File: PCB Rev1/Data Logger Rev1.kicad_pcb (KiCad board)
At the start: 2 copper layers, 4 parts, among them J1 MICRO_SD, U1 SAM-M10Q, U2 ESP32-PICO-V3-ZERO, U3 AP22653QW6-7

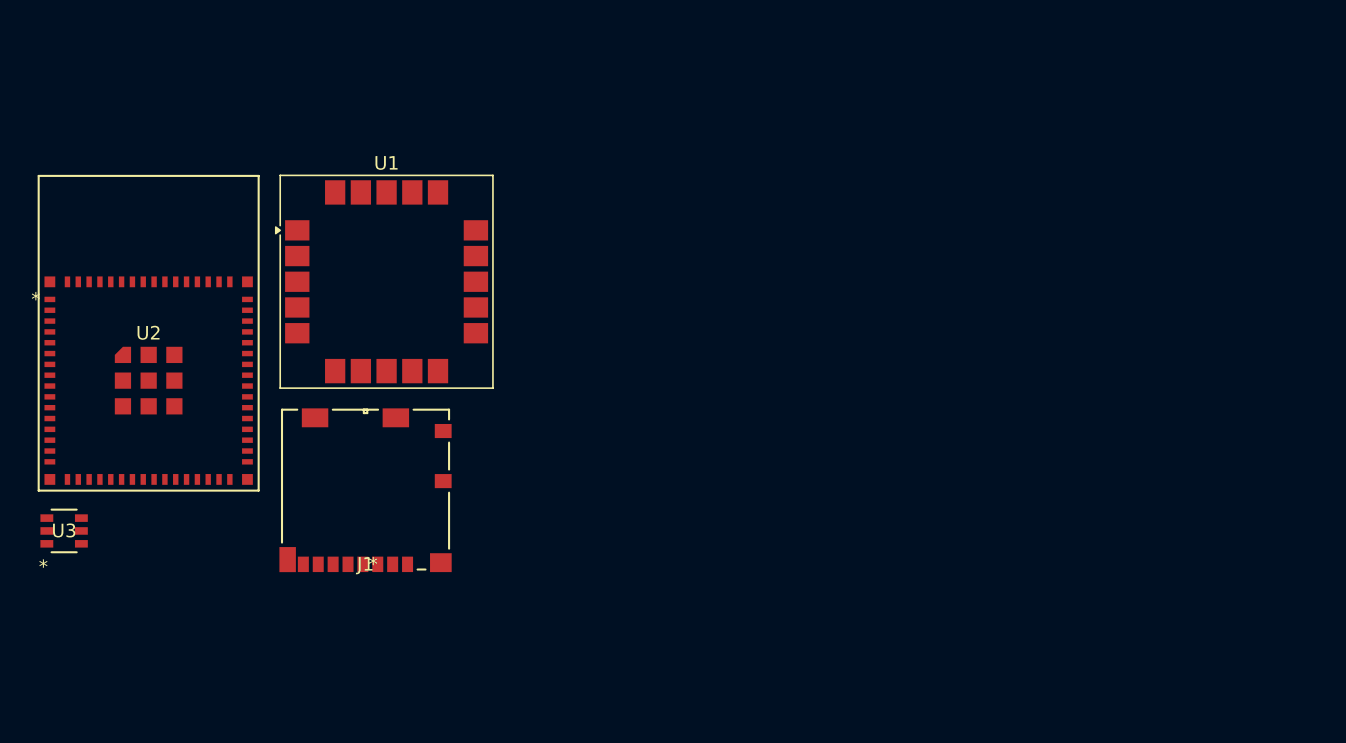
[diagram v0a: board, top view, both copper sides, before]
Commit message: aggregated SD card and switch, updated power architecture to use 5V, added TVS diode array
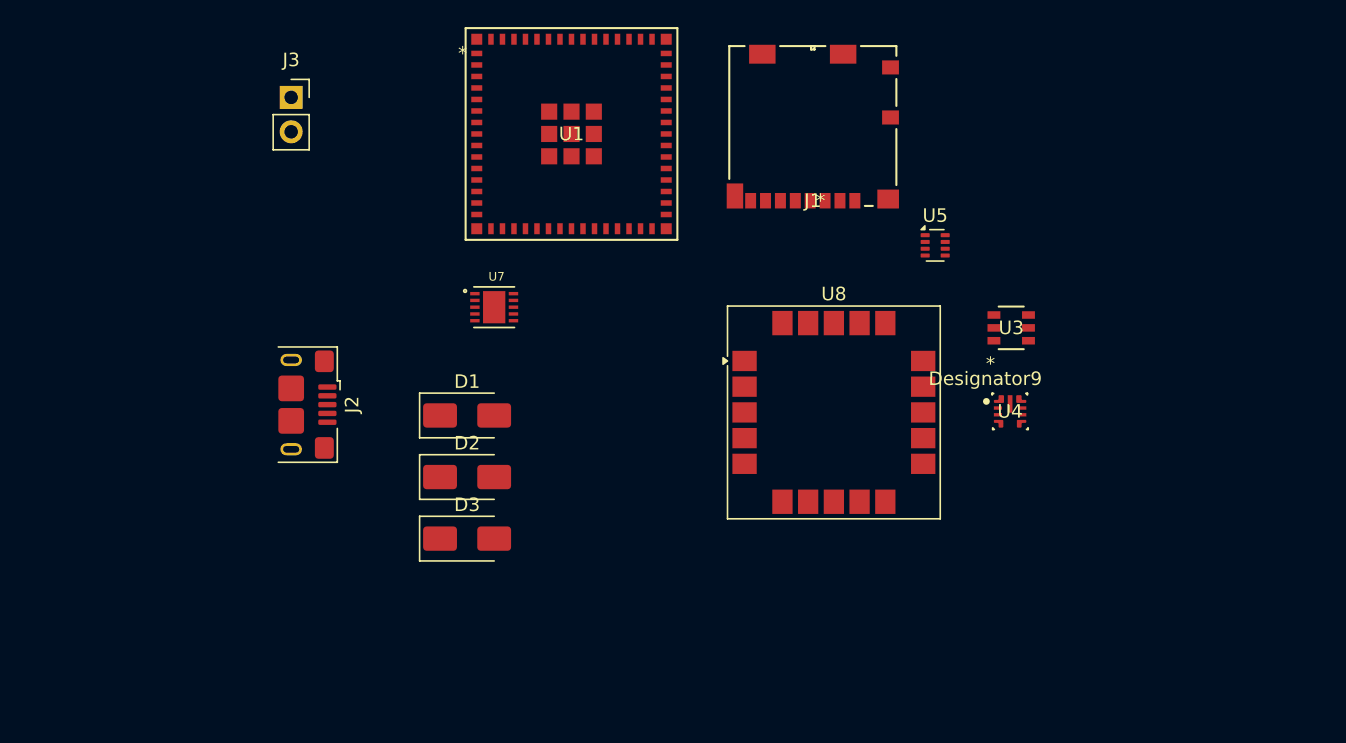
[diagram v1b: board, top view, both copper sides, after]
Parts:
- removed U2: ESP32-PICO-V3-ZERO, footprints:ESP32-PICO-V3-ZERO_EXP
- added D1: TVS, Diode_SMD:D_SMA, F.Cu at (144.5, 100.0)
- added D2: TVS, Diode_SMD:D_SMA, F.Cu at (144.5, 104.5)
- added D3: TVS, Diode_SMD:D_SMA, F.Cu at (144.5, 109.1)
- added J2: USB_B_Micro, Connector_USB:USB_Micro-B_Amphenol_10118193-0001LF_Horizontal, F.Cu at (131.5, 99.2)
- added J3: Conn_01x02_Socket, Connector_PinSocket_2.54mm:PinSocket_1x02_P2.54mm_Vertical, F.Cu at (131.5, 76.5)
- added U4: LMR43620MSC3RPERQ1, footprints:RPE0009A-MFG, F.Cu at (184.6, 99.7)
- added U5: TPS2116DRL, Package_TO_SOT_SMD:SOT-583-8, F.Cu at (179.1, 87.4)
- added U7: LT3042EDD_PBF, footprints:VREG_LT3042EDD_PBF, F.Cu at (146.5, 92.0)
- added U8: SAM-M10Q, RF_GPS:ublox_SAM-M8Q, F.Cu at (171.6, 99.8)
- U1: value SAM-M10Q -> ESP32-S3-MINI-1U-N8; footprint RF_GPS:ublox_SAM-M8Q -> footprints:ESP32-S3-MINI-1U_EXP
- moved U3 71.6 mm to (184.7, 93.5)
- moved J1 42.6 mm to (170.0, 78.6)
- moved U1 17.5 mm to (152.2, 79.2)
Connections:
- J1 pad 1: unconnected-(J1-DAT2-Pad1) -> /GPIO42
- J1 pad 10: unconnected-(J1-SW_DETECT-Pad10) -> GND
- J1 pad 2: unconnected-(J1-CD/DAT3-Pad2) -> /GPIO35
- J1 pad 3: unconnected-(J1-CMD-Pad3) -> /GPIO37
- J1 pad 4: unconnected-(J1-VDD-Pad4) -> /power_switch/out
- J1 pad 5: unconnected-(J1-CLK-Pad5) -> /GPIO36
- J1 pad 6: unconnected-(J1-VSS-Pad6) -> GND
- J1 pad 7: unconnected-(J1-DAT0-Pad7) -> /GPIO38
- J1 pad 8: unconnected-(J1-DAT1-Pad8) -> /GPIO39
- J1 pad 9: unconnected-(J1-SW_DETECT-Pad9) -> /GPIO1
- U1 pad 1: Net-(U1-GND-Pad1) -> Net-(U1-GND1-Pad1)
- U1 pad 10: Net-(U1-GND-Pad1) -> unconnected-(U1-IO6-Pad10)
- U1 pad 11: Net-(U1-GND-Pad1) -> unconnected-(U1-IO7-Pad11)
- U1 pad 15: Net-(U1-GND-Pad1) -> unconnected-(U1-IO11-Pad15)
- U1 pad 16: Net-(U1-GND-Pad1) -> unconnected-(U1-IO12-Pad16)
- U1 pad 2: unconnected-(U1-VCC_IO-Pad2) -> Net-(U1-GND1-Pad1)
- U1 pad 20: Net-(U1-GND-Pad1) -> unconnected-(U1-IO16-Pad20)
- U1 pad 4: Net-(U1-GND-Pad1) -> /GPIO0
- U1 pad 5: Net-(U1-GND-Pad1) -> /GPIO1
- U1 pad 6: Net-(U1-GND-Pad1) -> unconnected-(U1-IO2-Pad6)
- U3 pad 1: unconnected-(U3-in-Pad1) -> +3.3V
- U3 pad 2: unconnected-(U3-gnd-Pad2) -> GND
- U3 pad 3: unconnected-(U3-en-Pad3) -> /power_switch/en
- U3 pad 4: unconnected-(U3-*fault-Pad4) -> Net-(U3-*fault)
- U3 pad 5: unconnected-(U3-ilim-Pad5) -> Net-(U3-ilim)
- U3 pad 6: unconnected-(U3-out-Pad6) -> /power_switch/out

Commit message: added PCB rev2!
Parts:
- removed D2: TVS, Diode_SMD:D_SMA
- removed J1: MICRO_SD, footprints:104031-0811_MOL
- removed J3: Conn_01x02_Socket, Connector_PinSocket_2.54mm:PinSocket_1x02_P2.54mm_Vertical
- removed U7: LT3042EDD_PBF, footprints:VREG_LT3042EDD_PBF
- removed U8: SAM-M10Q, RF_GPS:ublox_SAM-M8Q
- added 12V: 12V_Tractor, footprints:PHOENIX_1725656, F.Cu at (205.3, 87.8)
- added 3.3V: 3.3V, footprints:TP_245X165, F.Cu at (179.7, 119.6)
- added 5V: 5V, footprints:TP_245X165, F.Cu at (199.4, 95.8)
- added 5V|3.7V: V_BAT_IC, footprints:TP_245X165, F.Cu at (199.4, 92.5)
- added BATT: BATTERY_PLUG, footprints:PHOENIX_1725656, F.Cu at (205.3, 106.3)
- added BOOT: BOOT, footprints:TP_245X165, F.Cu at (150.7, 81.0)
- added BOOT: BOOT, footprints:SW_TL1105TF160Q, F.Cu at (159.9, 83.3)
- added C1: 10uF, footprints:CAPC3216X190N, F.Cu at (192.1, 82.3)
- added C10: 4.7uF, Capacitor_SMD:C_0603_1608Metric, F.Cu at (191.9, 94.8)
- added C11: 10uF, Capacitor_SMD:C_0805_2012Metric, F.Cu at (155.2, 115.8)
- added C12: 0.1uF, Capacitor_SMD:C_0603_1608Metric, F.Cu at (157.2, 116.1)
- added C13: 10uF, Capacitor_SMD:C_0805_2012Metric, F.Cu at (192.6, 111.2)
- added C14: 1uF, Capacitor_SMD:C_0603_1608Metric, F.Cu at (193.9, 116.3)
- added C15: 10uF, Capacitor_SMD:C_0805_2012Metric, F.Cu at (186.8, 111.2)
- added C16: 10uF, Capacitor_SMD:C_0805_2012Metric, F.Cu at (182.2, 113.4)
- added C17: 0.1uF, Capacitor_SMD:C_0603_1608Metric, F.Cu at (180.2, 113.2)
- added C18: 0.1uF, Capacitor_SMD:C_0603_1608Metric, F.Cu at (176.0, 110.9)
- added C19: 0.1uF, Capacitor_SMD:C_0603_1608Metric, F.Cu at (178.7, 102.0)
- added C2: 4.7uF, footprints:CAPC2012X150N, F.Cu at (194.5, 90.8)
- added C20: 1uF, Capacitor_SMD:C_0603_1608Metric, F.Cu at (178.7, 98.8)
- added C21: 10uF, Capacitor_SMD:C_0805_2012Metric, F.Cu at (180.7, 102.2)
- added C22: 10uF, Capacitor_SMD:C_0805_2012Metric, F.Cu at (148.9, 119.5)
- added C23: 1uF, Capacitor_SMD:C_0603_1608Metric, F.Cu at (138.2, 119.5)
- added C3: 4.7uF, footprints:CAPC2012X150N, F.Cu at (192.6, 84.8)
- added C4: 100nF, footprints:CAPC2012X94N, F.Cu at (192.6, 87.0)
- added C5: 1uF, Capacitor_SMD:C_0805_2012Metric, F.Cu at (187.9, 90.5)
- added C6: 100nF, footprints:CAPC1005X55N, F.Cu at (188.9, 88.3)
- added C7: 22uF, footprints:CAPC3216X190N, F.Cu at (186.2, 80.5)
- added C8: 10uF, Capacitor_SMD:C_0805_2012Metric, F.Cu at (194.4, 98.8)
- added C9: 4.7uF, Capacitor_SMD:C_0603_1608Metric, F.Cu at (192.4, 102.8)
- added D4: LED, LED_SMD:LED_0603_1608Metric, F.Cu at (183.7, 94.5)
- added D5: LED, LED_SMD:LED_0603_1608Metric, F.Cu at (183.7, 103.5)
- added D6: LED, LED_SMD:LED_0603_1608Metric, F.Cu at (183.9, 99.0)
- added EN: EN, footprints:TP_245X165, F.Cu at (181.1, 91.6)
- added FB1: FerriteBead, Resistor_SMD:R_0603_1608Metric, F.Cu at (143.4, 119.8)
- added G***: LOGO, footprints:strawberry_silkscreen_small, F.Cu at (124.6, 89.5)
- added J4: MICRO_SD, footprints:104031-0811_MOL, F.Cu at (164.6, 113.9)
- added JP1: Jumper_2_Open, Jumper:SolderJumper-2_P1.3mm_Open_RoundedPad1.0x1.5mm, F.Cu at (154.7, 119.2)
- added L1: 330nH, footprints:WE-MAPI_2510, F.Cu at (196.1, 86.3)
- added L2: 2.2uH, Inductor_SMD:L_TDK_VLS6045EX_VLS6045AF, F.Cu at (185.0, 85.2)
- added R1: 10, footprints:RES_ERJ3EKF10R0V, F.Cu at (194.3, 89.0)
- added R10: 10k, Resistor_SMD:R_0402_1005Metric, F.Cu at (157.2, 103.5)
- added R11: 10k, Resistor_SMD:R_0603_1608Metric, F.Cu at (175.2, 117.4)
- added R12: 40k, footprints:RESC1005X35N, F.Cu at (173.2, 113.7)
- added R13: 10k, Resistor_SMD:R_0603_1608Metric, F.Cu at (180.5, 98.8)
- added R14: 10k, Resistor_SMD:R_0603_1608Metric, F.Cu at (178.7, 105.3)
- added R15: 10k, Resistor_SMD:R_0402_1005Metric, F.Cu at (166.7, 105.7)
- added R2: 1k, Resistor_SMD:R_0603_1608Metric, F.Cu at (189.9, 103.5)
- added R3: 10k, Resistor_SMD:R_0603_1608Metric, F.Cu at (188.1, 103.5)
- added R4: 470, Resistor_SMD:R_0603_1608Metric, F.Cu at (185.9, 94.0)
- added R5: 470, Resistor_SMD:R_0603_1608Metric, F.Cu at (185.7, 103.5)
- added R6: 470, Resistor_SMD:R_0603_1608Metric, F.Cu at (185.7, 97.3)
- added R7: 10k, Resistor_SMD:R_0402_1005Metric, F.Cu at (157.7, 101.0)
- added R8: 10k, Resistor_SMD:R_0402_1005Metric, F.Cu at (169.9, 105.8)
- added R9: 10k, Resistor_SMD:R_0402_1005Metric, F.Cu at (157.2, 106.5)
- added REF**: MountingHole_2.5mm_Pad, MountingHole:MountingHole_2.5mm_Pad, F.Cu at (120.7, 81.8)
- added REF**: MountingHole_2.5mm_Pad, MountingHole:MountingHole_2.5mm_Pad, F.Cu at (120.7, 118.3)
- added REF**: MountingHole_2.5mm_Pad, MountingHole:MountingHole_2.5mm_Pad, F.Cu at (202.9, 118.0)
- added RST: RESET, footprints:SW_TL1105TF160Q, F.Cu at (177.2, 83.3)
- added TH1: 10k, Resistor_SMD:R_0402_1005Metric, F.Cu at (187.9, 95.2)
- added TP3: RXD, footprints:TP_245X165, F.Cu at (157.9, 91.0)
- added TP6: TXD, footprints:TP_245X165, F.Cu at (157.9, 93.3)
- added U2: MCP73871-2CCI_ML, footprints:QFN50P400X400X100-21N, F.Cu at (189.7, 99.0)
- added U6: SAM-M10Q, RF_GPS:ublox_SAM-M8Q, F.Cu at (138.8, 99.8)
- added V_BAT: V_BAT, footprints:TP_245X165, F.Cu at (199.4, 99.0)
- D1: footprint Diode_SMD:D_SMA -> Diode_SMD:D_SOD-523
- D3: value TVS -> D_Schottky; footprint Diode_SMD:D_SMA -> footprints:CR_SMP_DO-220AA_VIS
- U1: value ESP32-S3-MINI-1U-N8 -> LMR43620MSC5-Q1RPE; footprint footprints:ESP32-S3-MINI-1U_EXP -> footprints:RPE0009A-MFG
- U3: value AP22653QW6-7 -> TPS7A4700RGWR; footprint footprints:SOT26-A1-AP22653Q_DIO -> footprints:QFN65P500X500X100-21N
- U4: value LMR43620MSC3RPERQ1 -> AP22653QW6-7; footprint footprints:RPE0009A-MFG -> footprints:SOT26-A1-AP22653Q_DIO
- U5: value TPS2116DRL -> ESP32-S3-MINI-1U-N8; footprint Package_TO_SOT_SMD:SOT-583-8 -> footprints:ESP32-S3-MINI-1U_EXP
- moved D3 58.3 mm to (196.1, 81.9)
- moved D1 52.6 mm to (193.1, 79.8), turned to 180 degrees
- moved J2 41.7 mm to (168.6, 80.3), turned to 180 degrees
- moved U1 40.4 mm to (191.2, 89.6), turned to 180 degrees
- moved U3 23.3 mm to (189.7, 116.3)
- moved U4 16.1 mm to (176.7, 113.8), turned to 180 degrees
- moved U5 13.1 mm to (169.3, 96.1), turned to 180 degrees
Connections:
- D1 pad 1: GND -> +12V
- D1 pad 2: /GPIO19 -> GND
- D3 pad 1: GND -> +12V
- D3 pad 2: +12V -> /12V_5V BUCK/PI_IN
- J2 pad 1: +12V -> +5V
- J2 pad 2: /GPIO19 -> /D-
- J2 pad 3: /GPIO20 -> /D+
- U1 pad 1: Net-(U1-GND1-Pad1) -> GND
- U1 pad 2: Net-(U1-GND1-Pad1) -> unconnected-(U1-PGOOD-Pad2)
- U1 pad 3: unconnected-(U1-3V3-Pad3) -> /12V_5V BUCK/V_IN_BUCK
- U1 pad 4: /GPIO0 -> /12V_5V BUCK/V_IN_BUCK
- U1 pad 5: /GPIO1 -> Net-(U1-SW)
- U1 pad 6: unconnected-(U1-IO2-Pad6) -> Net-(U1-BOOT)
- U1 pad 7: unconnected-(U1-IO3-Pad7) -> Net-(U1-VCC)
- U1 pad 8: unconnected-(U1-IO4-Pad8) -> +5V
- U1 pad 9: unconnected-(U1-IO5-Pad9) -> GND
- U3 pad 1: +3.3V -> /5V_3.3V LDO/3.3V
- U3 pad 2: GND -> (no net)
- U3 pad 3: /power_switch/en -> /5V_3.3V LDO/3.3V
- U3 pad 4: Net-(U3-*fault) -> unconnected-(U3-6P4V2-Pad4)
- U3 pad 5: Net-(U3-ilim) -> unconnected-(U3-6P4V1-Pad5)
- U3 pad 6: /power_switch/out -> unconnected-(U3-3P2V-Pad6)
- U4 pad 1: GND -> /5V_3.3V LDO/3.3V
- U4 pad 2: unconnected-(U4-PGOOD-Pad2) -> GND
- U4 pad 3: +12V -> /EN
- U4 pad 4: +12V -> Net-(U4-*FAULT)
- U4 pad 6: Net-(U4-BOOT) -> /EN_SWITCH/V_OUT
- U5 pad 1: unconnected-(U5-GND-Pad1) -> GND
- U5 pad 2: Net-(U5-VOUT-Pad2) -> GND
- U5 pad 3: /GPS Module/3.6V -> /5V_3.3V LDO/3.3V
- U5 pad 4: unconnected-(U5-PR1-Pad4) -> Net-(U5-IO0)
- U5 pad 7: Net-(U5-VOUT-Pad2) -> /EN
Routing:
- net /EN_SWITCH/V_OUT: track 0.00 -> 74.1 mm, vias 0 -> 6
- net /5V_3.3V LDO/3.3V: track 0.00 -> 56.7 mm, vias 0 -> 6
- net Net-(U5-IO0): track 0.00 -> 48.3 mm, vias 0 -> 3
- net /EXTINT: track 0.00 -> 47.8 mm, vias 0 -> 2
- net /1SEC: track 0.00 -> 46.8 mm, vias 0 -> 2
- net Net-(U6-VCC): track 0.00 -> 44.8 mm
- net +5V: track 0.00 -> 41.2 mm, vias 0 -> 9
- net Net-(U5-EN): track 0.00 -> 40.4 mm, vias 0 -> 3
- net Net-(JP1-B): track 0.00 -> 35.8 mm
- net /DAT1: track 0.00 -> 32.7 mm, vias 0 -> 2
- net /DAT3: track 0.00 -> 30.6 mm, vias 0 -> 2
- net /DAT0: track 0.00 -> 30.0 mm, vias 0 -> 2
- net /CMD: track 0.00 -> 29.3 mm, vias 0 -> 2
- net /DAT2: track 0.00 -> 29.2 mm, vias 0 -> 2
- net /CLK: track 0.00 -> 22.7 mm
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- added copper zone on In2.Cu, net +5V
- added copper zone on F.Cu, net /12V_5V BUCK/PI_IN
- added copper zone on F.Cu, net /12V_5V BUCK/V_IN_BUCK
- added copper zone on In2.Cu, net /5V_3.3V LDO/3.3V
- added copper zone on In2.Cu, net /5V_3.3V LDO/5V/3.7V
- added copper zone on B.Cu, net GND
- added copper zone on F.Cu, net GND
- added copper zone on In1.Cu, net GND
- added copper zone on In2.Cu, net GND
- added copper zone on F.Cu, net Net-(U1-SW)
- added copper zone on F.Cu, net Net-(U1-VCC)
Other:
- board outline added: 88.5 x 42.5 mm
- copper layers 2 -> 4
- board text added: "OAS Data Logger"
- board text added: "Rev1 8/20/25"
